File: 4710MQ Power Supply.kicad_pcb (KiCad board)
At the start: 2 copper layers, 40 x 75 mm, 24 parts, among them J1 Jack-DC, J2 ATX 4 Pin, J3 Molex 4 Pin, U1 MP1499GD-Z

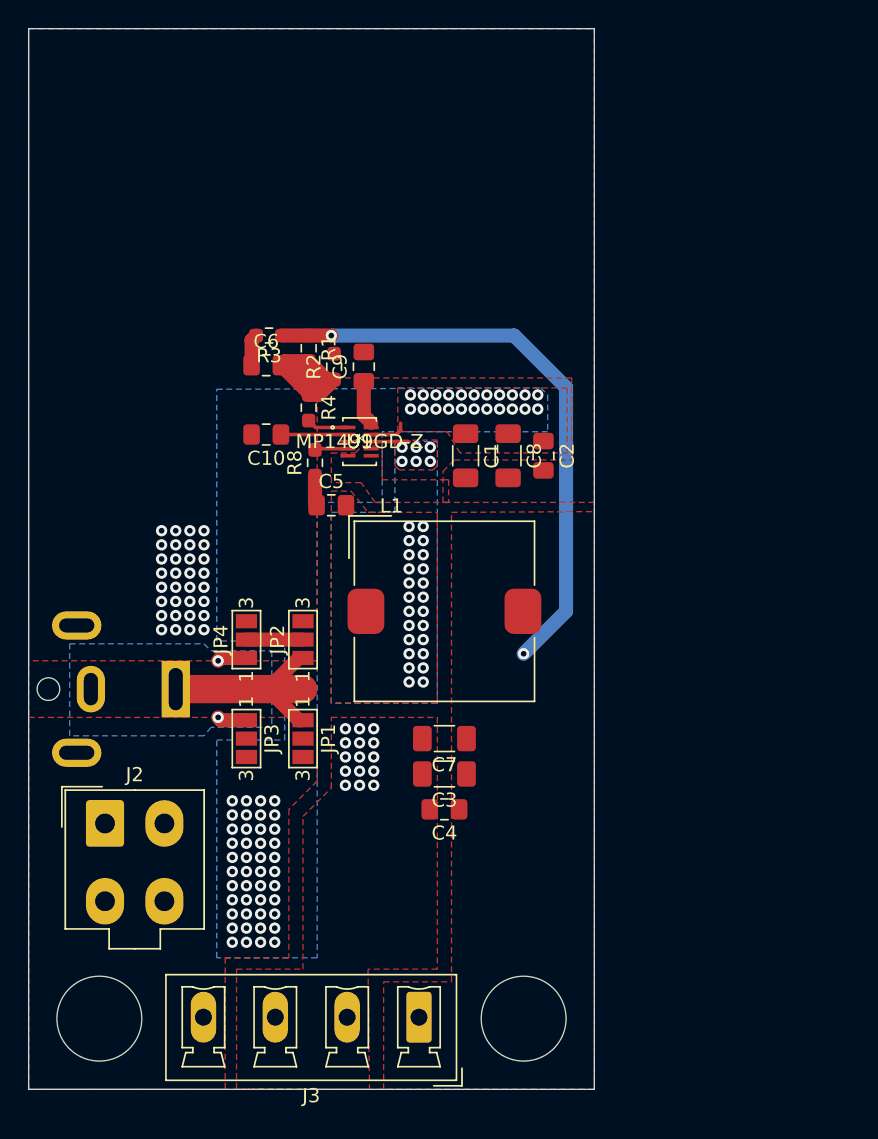
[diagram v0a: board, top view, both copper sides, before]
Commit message: Version 1.1
- Add DC-015 (Vertical DC Jack)
- Removed Jumpers (Innerside - +12V / Outside - GND fixed)
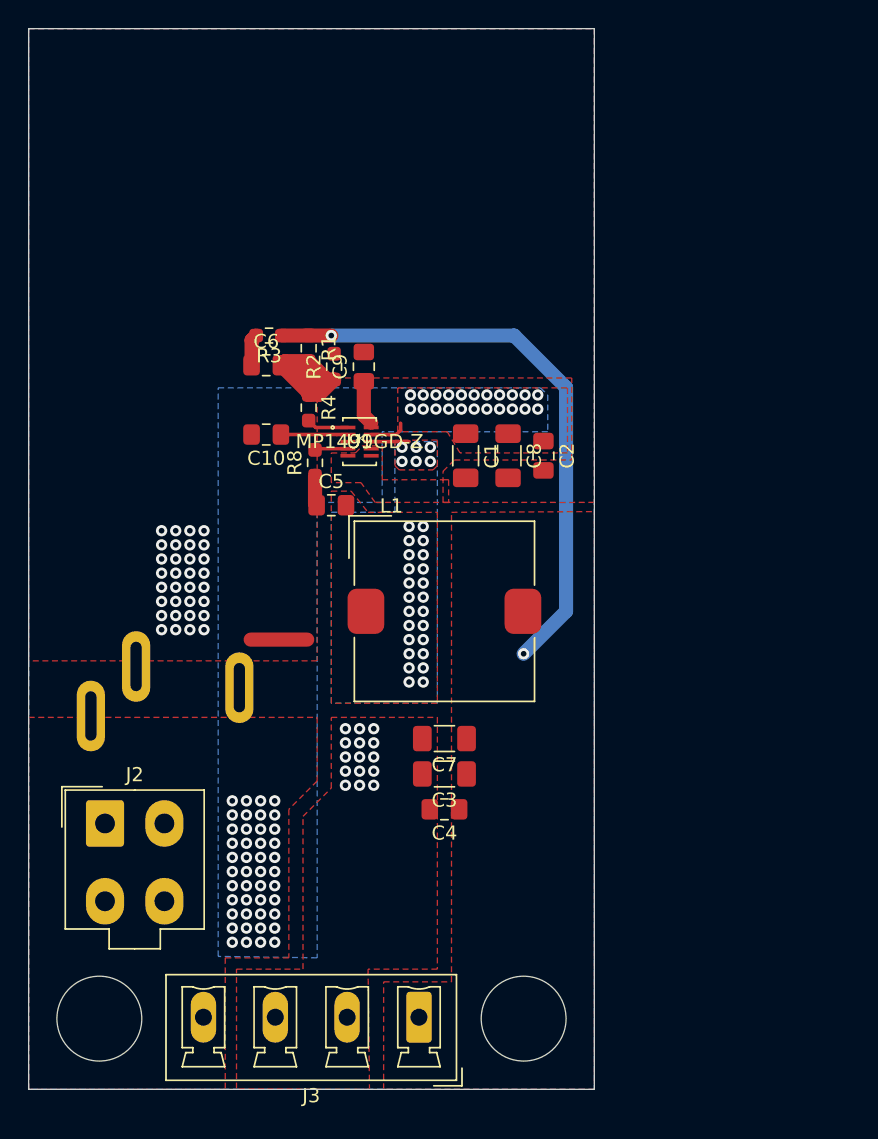
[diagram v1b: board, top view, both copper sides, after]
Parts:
- removed JP1: CTR_VDC, Jumper:SolderJumper-3_P1.3mm_Open_Pad1.0x1.5mm_NumberLabels
- removed JP2: CTR_GND, Jumper:SolderJumper-3_P1.3mm_Open_Pad1.0x1.5mm_NumberLabels
- removed JP3: OUT_VDC, Jumper:SolderJumper-3_P1.3mm_Open_Pad1.0x1.5mm_NumberLabels
- removed JP4: OUT_GND, Jumper:SolderJumper-3_P1.3mm_Open_Pad1.0x1.5mm_NumberLabels
- J1: footprint Connector_BarrelJack:BarrelJack_CUI_PJ-063AH_Horizontal -> DC015:DC015
- moved J1 0.51 mm to (133.5, 105.6)
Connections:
- J1 pad 1: /JACK_CTR -> +12V
- J1 pad 2: /JACK_OUT -> GND
- U1 pad 5: GND -> (no net)
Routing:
- net /JACK_CTR: track 16.3 -> 0.00 mm
- net /JACK_OUT: track 4.17 -> 0.00 mm, vias 2 -> 0
- removed copper zone on B.Cu, net /JACK_OUT

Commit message: [Not Completed] Version 1.2
- 3.3V LDO
- Current Sensor up to 30A
- UART to USB (CH340G)
- ADC 12bit
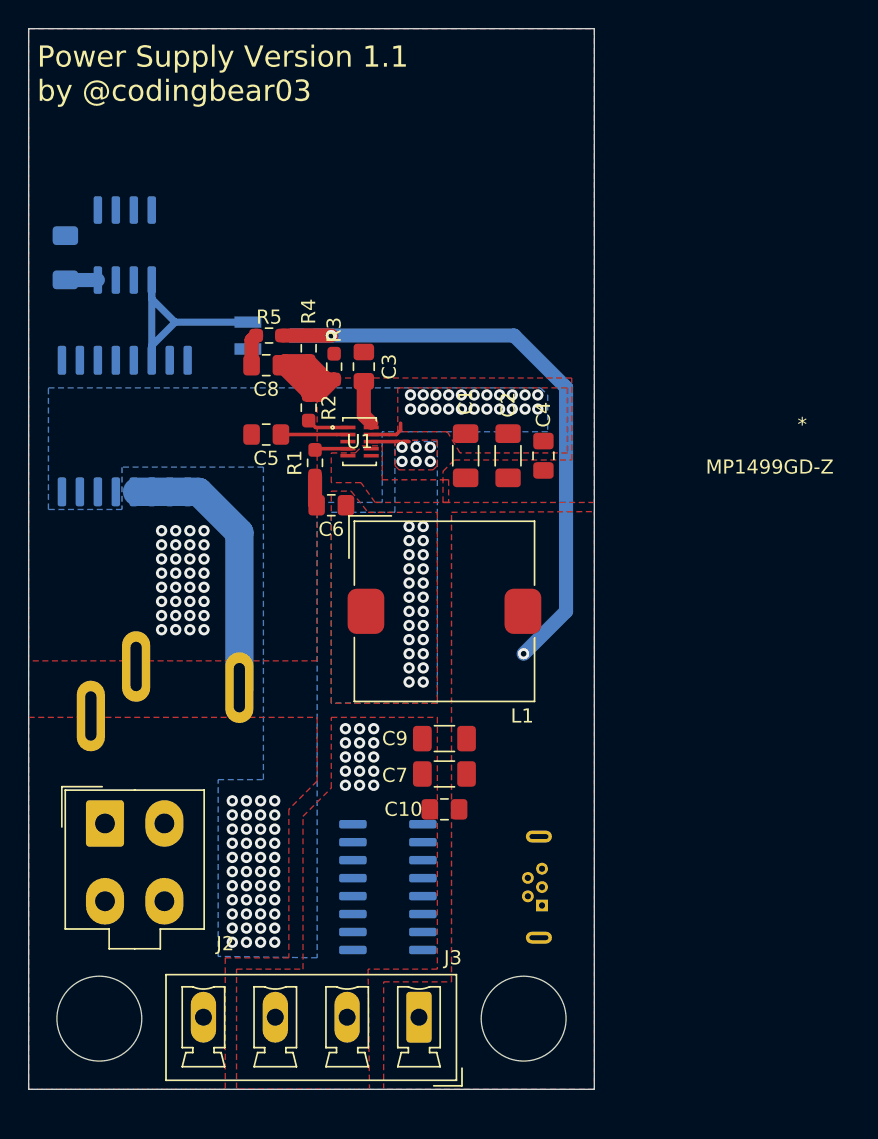
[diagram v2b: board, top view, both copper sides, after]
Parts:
- added C11: 4.7uF, Capacitor_SMD:C_1206_3216Metric_Pad1.33x1.80mm_HandSolder, B.Cu at (125.2, 75.2)
- added J4: USB_B_Micro, Connector_USB:USB_Micro-B_Wuerth_614105150721_Vertical, B.Cu at (158.9, 121.0)
- added U2: CH340G, Package_SO:SOIC-16_3.9x9.9mm_P1.27mm, B.Cu at (148.0, 119.7)
- added U3: LM1117-3.3, Package_TO_SOT_SMD:SOT-23_Handsoldering, B.Cu at (139.6, 80.7)
- added U4: ACS716xLATR-12BB-NL, Package_SO:SOIC-16W_7.5x10.3mm_P1.27mm, B.Cu at (129.4, 87.1)
- added U5: TSM1285BCSA, Package_SO:SOIC-8_3.9x4.9mm_P1.27mm, B.Cu at (129.4, 74.3)
- renumbered C4 to C10, C8 to C2, C9 to C3, C2 to C4, C10 to C5, C5 to C6, C3 to C7, C6 to C8, C7 to C9, R8 to R1, R4 to R2, R2 to R3, R1 to R4, R3 to R5
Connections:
- J1 pad 1: +12V -> VDC
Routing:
- net VDC: track 0.00 -> 19.4 mm
- net +3V3: track 0.00 -> 17.9 mm
- net GND: track 4.00 -> 0.00 mm
- net +5V: track 41.7 -> 44.6 mm
- net /ADC_REF: track 0.00 -> 2.28 mm
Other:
- board text added: "Power Supply Version 1.1 by @codingbear03"
